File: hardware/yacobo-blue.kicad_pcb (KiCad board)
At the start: 2 copper layers, 150 x 38 mm, 15 parts, among them J1 USB_B, J2 columns, J3 rows, J4 leds, M1 MountingHole_3.5mm, M2 MountingHole_3.5mm, M3 MountingHole_3.5mm, M4 MountingHole_3.5mm, U1 STM32F103C8T6

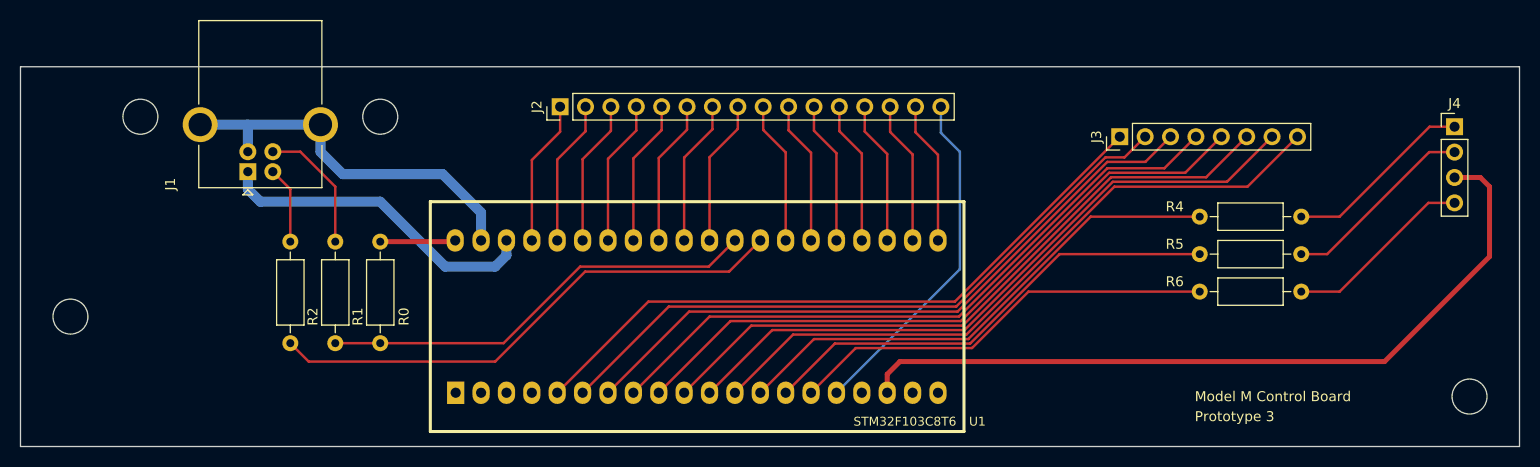
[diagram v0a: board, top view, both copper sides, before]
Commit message: add ground plane
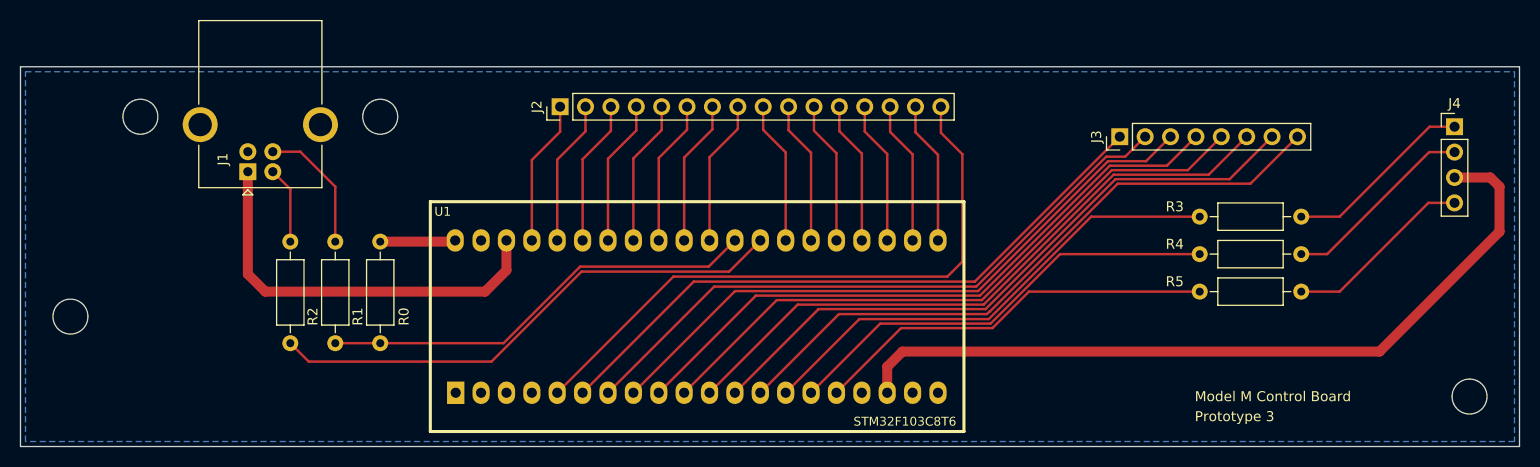
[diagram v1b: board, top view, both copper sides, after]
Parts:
- renumbered R4 to R3, R5 to R4, R6 to R5
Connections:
- U1 pad 10: row5 -> row4
- U1 pad 11: row6 -> row5
- U1 pad 12: row7 -> row6
- U1 pad 13: led0 -> row7
- U1 pad 14: led1 -> led0
- U1 pad 15: led2 -> led1
- U1 pad 16: col15 -> led2
- U1 pad 19: Net-(U1-Pad19) -> GND
- U1 pad 20: Net-(U1-Pad20) -> GND
- U1 pad 5: row0 -> col15
- U1 pad 6: row1 -> row0
- U1 pad 7: row2 -> row1
- U1 pad 8: row3 -> row2
- U1 pad 9: row4 -> row3
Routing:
- net GND: track 38.9 -> 0.00 mm
- net col15: track 34.5 -> 62.4 mm
- net +5V: track 32.8 -> 40.7 mm
- net led2: track 43.1 -> 40.5 mm
- net row6: track 66.9 -> 64.4 mm
- net row5: track 66.9 -> 64.4 mm
- net row4: track 66.9 -> 64.4 mm
- net row3: track 66.9 -> 64.4 mm
- net row2: track 66.9 -> 64.4 mm
- net row7: track 66.9 -> 64.4 mm
- net row1: track 66.9 -> 64.4 mm
- net row0: track 66.9 -> 64.4 mm
- net led1: track 47.2 -> 44.6 mm
- net led0: track 51.3 -> 48.7 mm
- net +3V3: track 77.9 -> 78.9 mm
- added copper zone on B.Cu, net GND
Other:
- net class Power added: clearance 0.2, trace_width 1, via_dia 0.8, via_drill 0.4

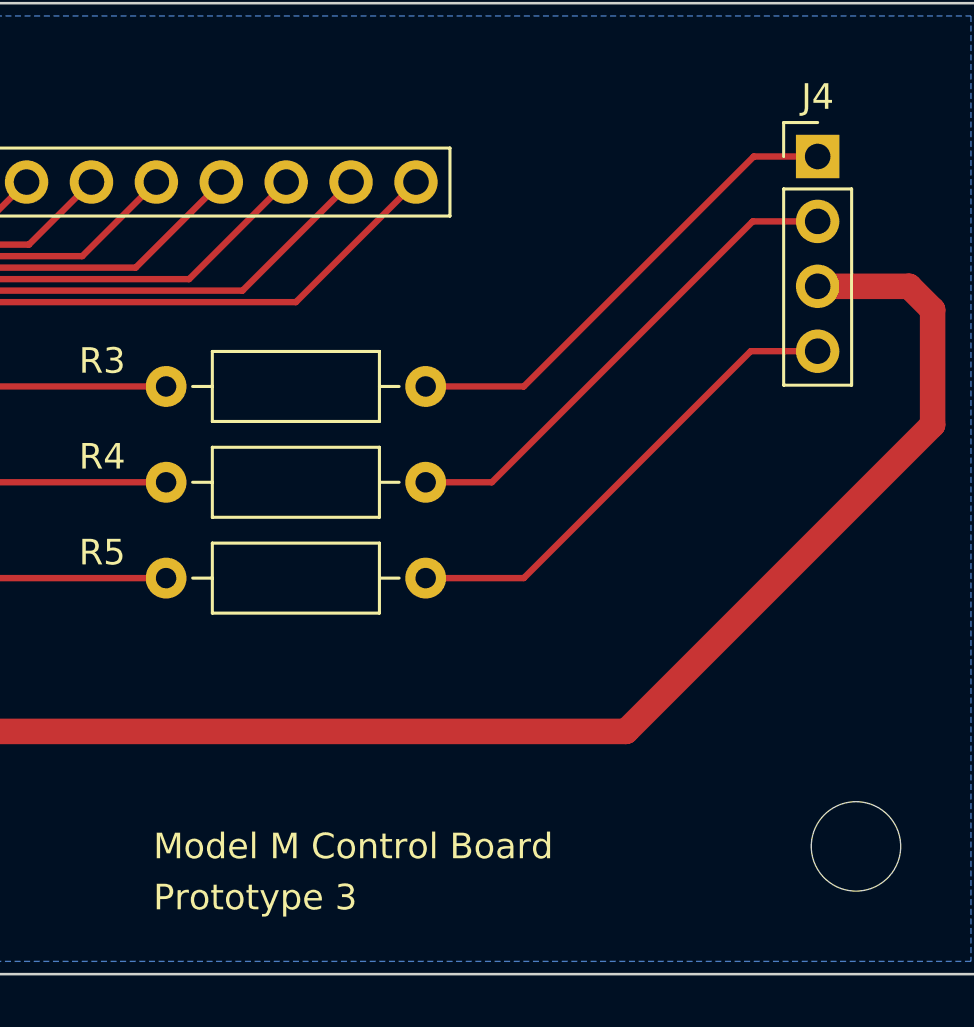
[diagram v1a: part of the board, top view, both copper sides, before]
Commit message: add reset code to keymap
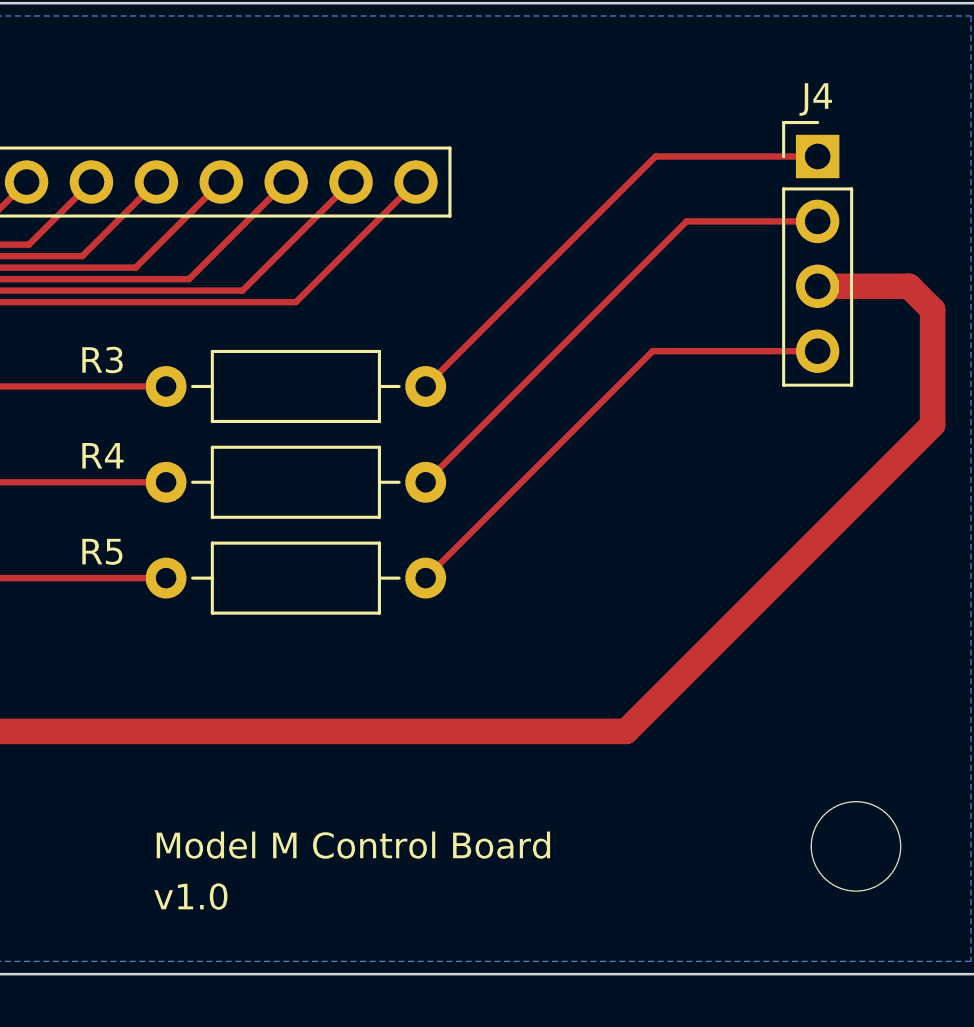
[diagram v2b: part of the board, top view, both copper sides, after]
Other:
- board text added: "v1.0"
- board text removed: "Prototype 3"
